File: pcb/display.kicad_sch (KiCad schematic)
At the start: 11 parts

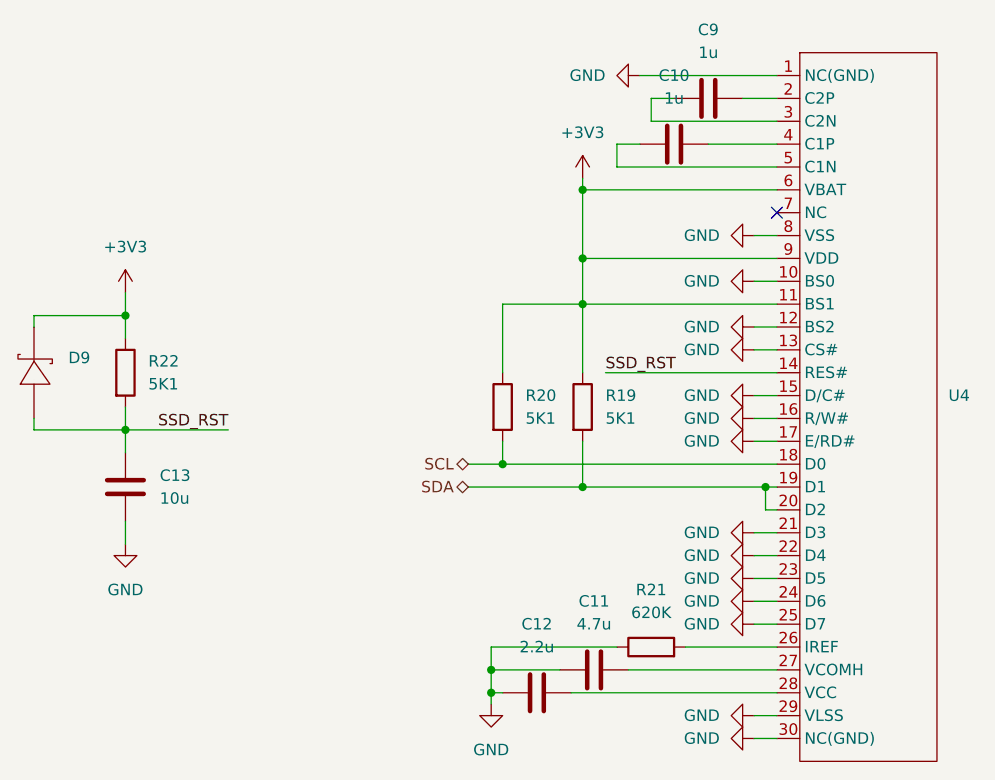
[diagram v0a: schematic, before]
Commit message: Connected reset pin to gpio2
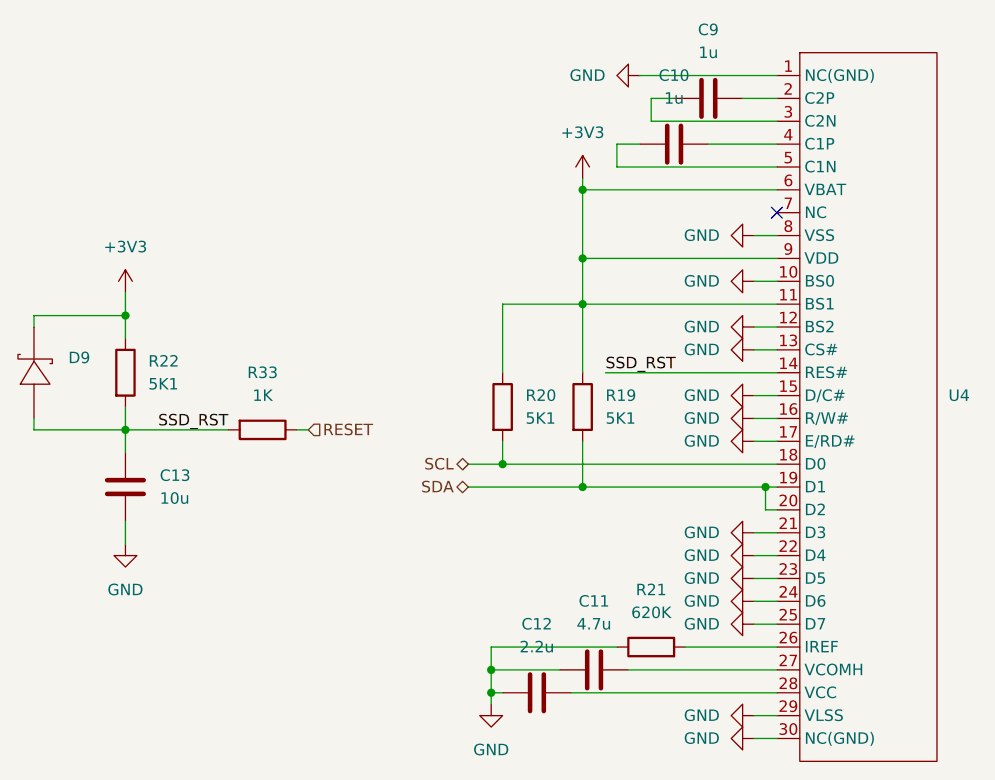
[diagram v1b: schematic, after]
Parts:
- added R33: 1K, Resistor_SMD:R_0603_1608Metric, symbol Device:R
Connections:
- net SSD_RST: now also R33.2
- new net RESET: R33.1
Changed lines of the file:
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@@
+	(wire
+		(pts
+			(xy 81.28 93.98) (xy 80.01 93.98)
+		)
+		(stroke
+			(width 0)
+			(type default)
+		)
+	)
 	(wire
 		(pts
@@
 		)
 	)
+	(hierarchical_label "RESET"
+		(shape input)
+		(at 81.28 93.98 0)
+		(effects
+			(font
+				(size 1.27 1.27)
+			)
+			(justify left)
+		)
+	)
 	(symbol
 		(lib_id "power:GND")
@@
 					(unit 1)
 				)
+			)
+		)
+	)
+	(symbol
+		(lib_id "Device:R")
+		(at 76.2 93.98 270)
+		(unit 1)
+		(exclude_from_sim no)
+		(in_bom yes)
+		(on_board yes)
+		(dnp no)
+		(fields_autoplaced yes)
+		(property "Reference" "R33"
+			(at 76.2 87.63 90)
+			(effects
+				(font
+					(size 1.27 1.27)
+				)
+			)
+		)
+		(property "Value" "1K"
+			(at 76.2 90.17 90)
+			(effects
+				(font
+					(size 1.27 1.27)
+				)
+			)
+		)
+		(property "Footprint" "Resistor_SMD:R_0603_1608Metric"
+			(at 76.2 92.202 90)
+			(effects
+				(font
+					(size 1.27 1.27)
+				)
+				(hide yes)
+			)
+		)
+		(property "Datasheet" "~"
+			(at 76.2 93.98 0)
+			(effects
+				(font
+					(size 1.27 1.27)
+				)
+				(hide yes)
+			)
+		)
+		(property "Description" "Resistor"
+			(at 76.2 93.98 0)
+			(effects
+				(font
+					(size 1.27 1.27)
+				)
+				(hide yes)
+			)
+		)
+		(property "Supplier Part" "C22548"
+			(at 76.2 93.98 0)
+			(effects
+				(font
+					(size 1.27 1.27)
+				)
+				(hide yes)
+			)
+		)
+		(pin "1"
+		)
+		(pin "2"
+		)
+		(instances
+			(project "capacitor-alarm-clock"
+				(path "/04b8bb56-25a8-431d-accc-900ca88fd18f/ebe10c23-19f6-433f-9285-78aaa5e0ae9a"
+					(reference "R33")
+					(unit 1)
+				)

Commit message: Upgrade kicad version to 10, add krita capacitor image
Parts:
- D9, U4: value ~ -> (none)

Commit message: Add JLC carts and BOM
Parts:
- C10, C9: Manufacturer Part (none) -> CL10B105KA8NNNC; Supplier (none) -> LCSC; Supplier Part C15849 -> C29936; Supplier Part URL (none) -> https://www.lcsc.com/product-detail/C29936.html
- C11: Manufacturer Part (none) -> CL10A475KO8NNNC; Supplier (none) -> LCSC; Supplier Part URL (none) -> https://www.lcsc.com/product-detail/C19666.html
- C12: Manufacturer Part (none) -> CL10A225KO8NNNC; Supplier (none) -> LCSC; Supplier Part URL (none) -> https://www.lcsc.com/product-detail/C23630.html
- C13: Manufacturer Part (none) -> CL10A106KP8NNNC; Supplier (none) -> LCSC; Supplier Part URL (none) -> https://www.lcsc.com/product-detail/C19702.html
- D9: Supplier Part URL (none) -> https://www.lcsc.com/product-detail/C82544.html
- R19, R20, R22: Manufacturer Part (none) -> FRC0603F5101TS; Supplier (none) -> LCSC; Supplier Part URL (none) -> https://www.lcsc.com/product-detail/C2907044.html
- R21: Manufacturer Part (none) -> 0603WAF6203T5E; Supplier (none) -> LCSC; Supplier Part URL (none) -> https://www.lcsc.com/product-detail/C23219.html
- R33: Manufacturer Part (none) -> RC0603FR-071KL; Supplier (none) -> LCSC; Supplier Part URL (none) -> https://www.lcsc.com/product-detail/C22548.html
- U4: Supplier Part URL (none) -> https://www.lcsc.com/product-detail/C18723026.html

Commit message: Update 10u capacitor to 25v rated one
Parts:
- C13: Manufacturer Part CL10A106KP8NNNC -> CL10A106MA8NRNC; Supplier Part C19702 -> C96446; Supplier Part URL https://www.lcsc.com/product-detail/C19702.html -> https://www.lcsc.com/product-detail/C96446.html
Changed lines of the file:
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@@
 			)
 		)
-		(property "Supplier Part" "C19702"
+		(property "Supplier Part" "C96446"
 			(at 60.96 100.33 0)
 			(hide yes)
@@
 			)
 		)
-		(property "Manufacturer Part" "CL10A106KP8NNNC"
+		(property "Manufacturer Part" "CL10A106MA8NRNC"
 			(at 60.96 100.33 0)
 			(hide yes)
@@
 			)
 		)
-		(property "Supplier Part URL" "https://www.lcsc.com/product-detail/C19702.html"
+		(property "Supplier Part URL" "https://www.lcsc.com/product-detail/C96446.html"
 			(at 60.96 100.33 0)
 			(hide yes)
